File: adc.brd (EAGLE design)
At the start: 100 x 80 mm, 1 part, among them U1 ADV7173KSTZ

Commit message: placa ADC v1
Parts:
- added C1, C10, C12, C3, C5, C6, C7, C8, C9: 10nf, eagle-ltspice:C0603
- added C11, C13, C2, C4: 10uf, eagle-ltspice:C0603
- added D1, D2, D3, D4, D5, D6: PMLL4150, diode:SOD80C
- added IC13, IC5, IC6: 4051D, 40xx:SO16
- added JP1, JP2, JP3: (no value), jumper:JP2
- added R1, R10, R11, R12, R13, R14, R15, R16, R17, R18, R19, R2, R20, R21, R22, R23, R24, R25, R26, R27, R28, R29, R3, R30, R31, R32, R33, R34, R35, R36, R37, R38, R39, R4, R40, R41, R42, R43, R44, R45, R46, R47, R5, R6, R7, R8, R9: (no value), SparkFun:0603
- added SV1, SV2: (no value), con-lstb:MA20-2
- added U$1, U$2: POT100K_3362U, SparkFun:3362U
- added U2, U5, U6, U7: AD5308ARUZ, Analog Devices_By_element14_Batch_1:SOP65P640X120-16N
- added U3: AD7927BRUZ, Analog Devices_By_element14_Batch_1:SOP65P640X120-20N
- added U4: ADV7173KSTZ, ADI-Phase-2:QFP50P900X900X160-48N
- moved U1 30.4 mm to (19.1, 29.5), turned to 180 degrees
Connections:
- net VAA_3 renamed +IN_B
- removed net ALOHADANCE: U1.1
- removed net VAA: U1.46
- removed net VAA_4: U1.19
- removed net VAA_5: U1.27
- removed net VAA_6: U1.30
- removed net VAA_7: U1.32
- removed net VAA_8: U1.34
- new net +2,5V_ADCREF: U1.5, U1.7, U4.5, U4.7
- new net +INA: U2.3
- new net CH_A(ADC): D1.A, D2.C, R17.1, U1.2, U5.10
- new net CH_B(ADC): D3.A, D4.C, R33.1, U4.11, U6.10
- new net CH_C(ADC): D5.A, D6.C, R47.1, U4.2, U7.10
- new net DAC_OUT: R1.2, U$1.P$3, U2.1
- new net DCLK: U1.14, U1.47, U4.14, U4.47
- new net DFS/GAIN: JP1.2, U1.4, U4.4
- new net DGND: C12.2, C13.2, C3.2, C4.2, C5.2, JP1.3, JP2.3, JP3.3, U1.1, U1.12, U1.16, U1.27, U1.29, U1.32, U1.34, U1.45, U3.17, U3.2, U3.20, U3.3, U4.1, U4.12, U4.16, U4.27, U4.29, U4.32, U4.34, U4.45
- new net GND: C1.2, C10.2, C11.2, C2.2, C7.2, C9.2, D2.A, D4.A, D6.A, IC13.8, IC5.8, IC6.8, R19.2, R22.2, R32.2, R36.2, R46.2, R8.2, U1.3, U2.14, U4.3
- new net N$1: C7.1, R2.1, U2.5
- new net N$10: SV2.29, U1.42
- new net N$100: U5.1, U5.2
- new net N$101: R31.1, R32.1, U6.11
- new net N$102: R37.2, R38.2, R39.2, R40.2, R41.2, R42.2, R43.2, R44.2
- new net N$103: U6.1, U6.2
- new net N$104: R45.1, R46.1, U7.11
- new net N$105: U7.1, U7.2
- new net N$106: R35.1, U7.3
- new net N$107: R21.1, U6.3
- new net N$109: R20.2, R21.2, R34.2, R35.2, R6.2, R7.2, U$2.P$3, U2.16
- new net N$11: SV2.40, U1.24
- new net N$12: SV2.30, U1.19
- new net N$13: SV2.32, U1.20
- new net N$14: SV2.39, U1.37
- new net N$15: SV2.31, U1.41
- new net N$16: SV2.25, U1.44
- new net N$17: SV2.34, U1.21
- new net N$18: SV2.27, U1.43
- new net N$19: SV2.35, U1.39
- new net N$2: C6.1, R1.1, R2.2
- new net N$20: SV2.37, U1.38
- new net N$21: SV2.36, U1.22
- new net N$22: SV2.28, U1.18
- new net N$23: SV2.26, U1.17
- new net N$24: SV2.2, U3.4
- new net N$25: SV2.38, U1.23
- new net N$26: SV2.4, U3.5
- new net N$27: SV2.6, U3.6
- new net N$28: SV2.8, U3.7
- new net N$29: SV2.10, U3.8
- new net N$3: C5.1, U$1.P$1, U$1.P$2, U2.2, U3.1
- new net N$30: SV2.12, U3.9
- new net N$31: SV2.14, U3.10
- new net N$32: SV2.16, U3.11
- new net N$33: SV2.18, U3.12
- new net N$34: SV2.20, U3.13
- new net N$35: SV2.22, U3.14
- new net N$36: SV2.24, U3.15
- new net N$37: SV2.1, U3.16
- new net N$38: IC5.13, R9.1
- new net N$39: IC5.14, R10.1
- new net N$4: C6.2, R3.2, U2.6, U2.7
- new net N$40: IC5.15, R11.1
- new net N$41: IC5.1, R12.1
- new net N$42: IC5.12, R13.1
- new net N$43: IC5.5, R14.1
- new net N$44: IC5.2, R15.1
- new net N$45: IC5.4, R16.1
- new net N$46: IC6.13, R23.1
- new net N$47: IC6.14, R24.1
- new net N$48: R23.2, R24.2, R25.2, R26.2, R27.2, R28.2, R29.2, R30.2
- new net N$49: R10.2, R11.2, R12.2, R13.2, R14.2, R15.2, R16.2, R9.2
- new net N$5: C9.1, R4.1, U2.12
- new net N$50: R18.1, R19.1, U5.11
- new net N$51: IC5.3, R17.2, U5.12
- new net N$52: IC6.15, R25.1
- new net N$53: IC6.1, R26.1
- new net N$54: IC6.12, R27.1
- new net N$55: IC6.5, R28.1
- new net N$56: IC6.2, R29.1
- new net N$57: IC6.4, R30.1
- new net N$58: R31.2, U6.6, U6.7
- new net N$59: R45.2, U7.6, U7.7
- new net N$6: C8.1, R3.1, R4.2
- new net N$60: IC13.3, R47.2, U7.12
- new net N$61: IC6.3, R33.2, U6.12
- new net N$62: IC13.13, R37.1
- new net N$63: IC13.14, R38.1
- new net N$64: IC13.15, R39.1
- new net N$65: IC13.1, R40.1
- new net N$66: IC13.12, R41.1
- new net N$67: IC13.5, R42.1
- new net N$68: IC13.2, R43.1
- new net N$69: IC13.4, R44.1
- new net N$7: C8.2, R5.2, U2.10, U2.11
- new net N$70: R34.1, R36.1, U7.5
- new net N$71: R6.1, R8.1, U5.5
- new net N$72: R20.1, R22.1, U6.5
- new net N$73: R7.1, U5.3
- new net N$74: SV1.33, U4.40
- new net N$75: SV1.29, U4.42
- new net N$76: SV1.40, U4.24
- new net N$77: SV1.30, U4.19
- new net N$78: SV1.32, U4.20
- new net N$79: SV1.39, U4.37
- new net N$8: R5.1, U$2.P$1, U$2.P$2, U2.15
- new net N$80: SV1.31, U4.41
- new net N$81: SV1.25, U4.44
- new net N$82: SV1.34, U4.21
- new net N$83: SV1.27, U4.43
- new net N$84: SV1.35, U4.39
- new net N$85: SV1.37, U4.38
- new net N$86: SV1.36, U4.22
- new net N$87: SV1.28, U4.18
- new net N$88: SV1.26, U4.17
- new net N$89: SV1.38, U4.23
- new net N$9: SV2.33, U1.40
- new net N$90: IC5.9, SV2.3
- new net N$91: IC5.10, SV2.5
- new net N$92: IC5.11, SV2.7
- new net N$93: IC13.9, SV1.1
- new net N$94: IC13.10, SV1.3
- new net N$95: IC13.11, SV1.5
- new net N$96: IC6.9, SV1.7
- new net N$97: IC6.10, SV1.9
- new net N$98: IC6.11, SV1.11
- new net N$99: R18.2, U5.6, U5.7
- new net S1: JP2.2, U1.8, U4.8
- new net S2: JP3.2, U1.9, U4.9
- new net VCC: C1.1, C10.1, C11.1, C2.1, D1.C, D3.C, D5.C, IC13.16, IC13.6, IC5.16, IC5.6, IC6.16, IC6.6, U1.13, U1.30, U1.31, U1.48, U4.13, U4.31, U4.48
- new net VD1: U4.30
- new net VDD: C12.1, C13.1, C3.1, C4.1, JP1.1, JP2.1, JP3.1, U1.15, U1.28, U1.33, U1.46, U2.13, U2.4, U3.18, U3.19, U4.15, U4.28, U4.33, U4.46, U5.13, U5.4, U6.13, U6.4, U7.13, U7.4
- new net VEE: IC13.7, IC5.7, IC6.7
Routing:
- net DGND: track 0.00 -> 92.1 mm
- net VDD: track 0.00 -> 87.1 mm, vias 0 -> 4
- net N$109: track 0.00 -> 78.7 mm
- net GND: track 0.00 -> 73.3 mm, vias 0 -> 3
- net S2: track 0.00 -> 71.0 mm, vias 0 -> 1
- net DFS/GAIN: track 0.00 -> 70.1 mm, vias 0 -> 1
- net CH_B(ADC): track 0.00 -> 65.1 mm, vias 0 -> 1
- net N$102: track 0.00 -> 45.2 mm
- net CH_C(ADC): track 0.00 -> 44.8 mm, vias 0 -> 2
- net CH_A(ADC): track 0.00 -> 43.2 mm
- net N$48: track 0.00 -> 40.6 mm
- net N$73: track 0.00 -> 37.0 mm, vias 0 -> 2
- net VCC: track 0.00 -> 34.0 mm
- net N$51: track 0.00 -> 33.0 mm, vias 0 -> 2
- net N$60: track 0.00 -> 31.4 mm, vias 0 -> 2
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- added copper zone on layer 1, net GND

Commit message: VHDL
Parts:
- removed D1, D2, D3, D4, D5, D6: PMLL4150, diode:SOD80C
- moved SV2 26.2 mm to (50.5, 2.54)
- moved JP3 25.5 mm to (30.0, 47.2), turned to 90 degrees
- moved JP1 19.9 mm to (25.9, 47.2), turned to 90 degrees
- moved JP2 15.0 mm to (21.8, 47.2), turned to 90 degrees
- moved SV1 14.7 mm to (4.57, 54.9)
- moved R17 13.1 mm to (51.3, 22.1)
- moved R18 13.0 mm to (57.1, 22.1)
- moved U5 12.8 mm to (53.8, 29.0)
- moved R19 12.2 mm to (54.4, 20.8)
- moved C4 11.3 mm to (19.1, 57.7)
- moved C3 10.6 mm to (21.1, 57.7)
- moved C1 10.6 mm to (35.3, 56.6)
- moved U$1 10.2 mm to (60.7, 21.8)
- moved C2 10.1 mm to (37.3, 56.6)
- moved C13 9.81 mm to (18.8, 31.2)
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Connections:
- removed net N$85: SV1.37, U4.38
- removed net N$92: IC5.11, SV2.7
- new net +5V: SV1.30, SV2.30, U2.4, U5.4, U6.4, U7.4
- new net -5V: U2.13, U5.13, U6.13, U7.13
- new net N$110: IC5.11, SV2.20
- new net N$111: SV2.16, U3.16
- net CH_A(ADC): no longer D1.A, D2.C
- net CH_B(ADC): no longer D3.A, D4.C
- net CH_C(ADC): no longer D5.A, D6.C
- net DGND: now also SV1.11, SV1.12, SV2.11, SV2.12
- net GND: no longer D2.A, D4.A, D6.A
- net N$10: now also SV2.25; no longer SV2.29
- net N$11: now also SV2.39; no longer SV2.40
- net N$12: now also SV2.32; no longer SV2.30
- net N$13: now also SV2.34; no longer SV2.32
- net N$14: now also SV2.37; no longer SV2.39
- net N$15: now also SV2.27; no longer SV2.31
- net N$16: now also SV2.21; no longer SV2.25
- net N$17: now also SV2.36; no longer SV2.34
- net N$18: now also SV2.23; no longer SV2.27
- net N$19: now also SV2.33; no longer SV2.35
- net N$20: now also SV2.35; no longer SV2.37
- net N$21: now also SV2.38; no longer SV2.36
- net N$24: now also SV2.13; no longer SV2.2
- net N$25: now also SV2.40; no longer SV2.38
- net N$26: now also SV2.9; no longer SV2.4
- net N$27: now also SV2.7; no longer SV2.6
- net N$28: now also SV2.5; no longer SV2.8
- net N$29: now also SV2.3; no longer SV2.10
- net N$30: now also SV2.1; no longer SV2.12
- net N$31: now also SV2.2; no longer SV2.14
- net N$32: now also SV2.4; no longer SV2.16
- net N$33: now also SV2.6; no longer SV2.18
- net N$34: now also SV2.8; no longer SV2.20
- net N$35: now also SV2.10; no longer SV2.22
- net N$36: now also SV2.14; no longer SV2.24
- net N$37: now also SV1.38, U4.37; no longer SV2.1, U3.16
- net N$74: now also SV1.40, U4.38; no longer SV1.33, U4.40
- net N$75: now also SV1.39, U4.39; no longer SV1.29, U4.42
- net N$76: now also SV1.36; no longer SV1.40
- net N$77: now also SV1.24; no longer SV1.30
- net N$78: now also SV1.26; no longer SV1.32
- net N$79: now also SV1.37, U4.40; no longer SV1.39, U4.37
- net N$80: now also SV1.35; no longer SV1.31
- net N$81: now also SV1.33, U4.42; no longer SV1.25, U4.44
- net N$82: now also SV1.28; no longer SV1.34
- net N$83: now also SV1.31; no longer SV1.27
- net N$84: now also SV1.27, U4.44; no longer SV1.35, U4.39
- net N$86: now also SV1.32; no longer SV1.36
- net N$87: now also SV1.22; no longer SV1.28
- net N$88: now also SV1.20; no longer SV1.26
- net N$89: now also SV1.34; no longer SV1.38
- net N$9: now also SV2.31; no longer SV2.33
- net N$90: now also SV2.24; no longer SV2.3
- net N$91: now also SV2.22; no longer SV2.5
- net N$93: now also SV1.19; no longer SV1.1
- net N$94: now also SV1.15; no longer SV1.3
- net N$95: now also SV1.13; no longer SV1.5
- net N$96: now also SV1.25; no longer SV1.7
- net N$97: now also SV1.23; no longer SV1.9
- net N$98: now also SV1.21; no longer SV1.11
- net VCC: no longer D1.C, D3.C, D5.C
- net VDD: now also SV1.29, SV2.29; no longer U2.13, U2.4, U5.13, U5.4, U6.13, U6.4, U7.13, U7.4
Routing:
- net +5V: track 0.00 -> 248.5 mm, vias 0 -> 4
- net VDD: track 87.1 -> 295.7 mm, vias 4 -> 5
- net VCC: track 34.0 -> 238.2 mm, vias 0 -> 12
- net DGND: track 92.1 -> 275.2 mm, vias 0 -> 5
- net VEE: track 0.00 -> 139.6 mm, vias 0 -> 3
- net GND: track 73.3 -> 169.2 mm, vias 3 -> 12
- net N$23: track 0.00 -> 86.8 mm
- net N$22: track 0.00 -> 81.2 mm
- net N$98: track 0.00 -> 80.7 mm, vias 0 -> 1
- net -5V: track 0.00 -> 79.5 mm, vias 0 -> 4
- net N$97: track 0.00 -> 74.9 mm, vias 0 -> 1
- net N$12: track 0.00 -> 71.8 mm
- net N$96: track 0.00 -> 71.6 mm, vias 0 -> 1
- net N$84: track 0.00 -> 71.3 mm
- net N$93: track 0.00 -> 70.4 mm
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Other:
- board size 100 x 80 mm -> 87.6 x 89.9 mm

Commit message: autalização
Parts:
- added X1: (no value), con-ptr500:AK300/5
- moved SV1 3.90 mm to (1.27, 56.9)
- moved U4 3.58 mm to (24.5, 61.3)
- moved C3 3.16 mm to (18.2, 58.9)
- moved C4 3.16 mm to (16.1, 58.9)
- moved C1 3.14 mm to (32.4, 57.8)
- moved C2 3.14 mm to (34.4, 57.8)
- moved C5 2.40 mm to (59.9, 21.8), turned to 180 degrees
- moved R29 2.34 mm to (46.5, 52.1)
- moved R30 1.89 mm to (46.4, 54.2)
- moved IC6 1.76 mm to (39.3, 48.4)
- moved R28 1.49 mm to (46.4, 56.3)
- moved R26 1.22 mm to (45.9, 48.5)
- moved C13 1.12 mm to (19.8, 30.7)
- moved C12 0.92 mm to (21.6, 30.7)
- moved U1 0.89 mm to (27.7, 32.6)
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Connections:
- removed net DGND: C12.2, C13.2, C3.2, C4.2, C5.2, JP1.3, JP2.3, JP3.3, SV1.11, SV1.12, SV2.11, SV2.12, U1.1, U1.12, U1.16, U1.27, U1.29, U1.32, U1.34, U1.45, U3.17, U3.2, U3.20, U3.3, U4.1, U4.12, U4.16, U4.27, U4.29, U4.32, U4.34, U4.45
- net +2,5V_ADCREF: now also X1.3
- net +5V: now also X1.5
- net -5V: now also X1.4
- net DCLK: now also SV1.10
- net GND: now also C12.2, C13.2, C3.2, C4.2, C5.2, JP1.3, JP2.3, JP3.3, SV1.11, SV1.29, SV2.11, SV2.29, U1.1, U1.12, U1.16, U1.27, U1.29, U1.32, U1.34, U1.45, U3.17, U3.2, U3.20, U3.3, U4.1, U4.12, U4.27, U4.29, U4.32, U4.34, U4.45, X1.1
- net N$93: now also SV1.17; no longer SV1.19
- net VDD: now also SV1.12, SV2.12, X1.2; no longer SV1.29, SV2.29
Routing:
- net GND: track 169.2 -> 475.0 mm, vias 12 -> 19
- net DGND: track 275.2 -> 0.00 mm, vias 5 -> 0
- net -5V: track 79.5 -> 142.3 mm
- net +5V: track 248.5 -> 309.9 mm
- net DCLK: track 68.3 -> 115.1 mm, vias 2 -> 3
- net VDD: track 295.7 -> 335.1 mm
- net +2,5V_ADCREF: track 45.6 -> 79.7 mm, vias 2 -> 4
- net N$102: track 45.2 -> 18.5 mm
- net VEE: track 139.6 -> 161.6 mm
- net S2: track 59.2 -> 41.2 mm
- net N$48: track 35.6 -> 19.2 mm
- net N$95: track 64.4 -> 72.4 mm
- net N$23: track 86.8 -> 94.6 mm
- net N$98: track 80.7 -> 87.4 mm
- net N$94: track 67.1 -> 73.6 mm
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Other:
- board size 87.6 x 89.9 mm -> 96.2 x 95.5 mm

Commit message: Atualização
VHDL com SWITCH CASE. 1-16 start end package
C# com controle de erro
ADC com alterações
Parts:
- removed X1: (no value), con-ptr500:AK300/5
- added X2: (no value), con-ptr500:AK300/6
- moved R45 3.84 mm to (54.1, 63.0), turned to 180 degrees
- moved C13 3.07 mm to (19.8, 27.6)
- moved R33 1.81 mm to (50.7, 41.9)
- moved R21 1.78 mm to (66.5, 54.4)
- moved R46 1.30 mm to (56.6, 65.5)
- moved R12 1.24 mm to (44.7, 22.1)
- moved R14 1.24 mm to (44.7, 29.4)
- moved R15 1.24 mm to (44.7, 24.6)
- moved R16 1.24 mm to (44.7, 27.2)
- moved R20 1.22 mm to (66.5, 50.7)
- moved R22 1.19 mm to (62.7, 50.7)
- moved C12 0.54 mm to (21.1, 30.7)
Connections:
- removed net N$100: U5.1, U5.2
- removed net N$103: U6.1, U6.2
- removed net N$105: U7.1, U7.2
- removed net VD1: U4.30
- new net 1V: U3.19, X2.2
- net +2,5V_ADCREF: now also X2.3; no longer X1.3
- net +5V: now also SV1.12, SV2.12, X2.5; no longer SV1.30, SV2.30, X1.5
- net -5V: now also X2.4; no longer X1.4
- net GND: now also X2.1; no longer X1.1
- net N$102: now also U7.1, U7.2
- net N$110: now also SV2.15; no longer SV2.20
- net N$48: now also U6.1, U6.2
- net N$49: now also U5.1, U5.2
- net N$90: now also SV2.19; no longer SV2.24
- net N$91: now also SV2.17; no longer SV2.22
- net VCC: now also U4.30
- net VDD: now also SV1.30, SV2.30, X2.6; no longer SV1.12, SV2.12, U3.19, X1.2
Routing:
- net GND: track 475.0 -> 1079.7 mm, vias 19 -> 21
- net VCC: track 244.6 -> 463.0 mm, vias 10 -> 11
- net 1V: track 0.00 -> 119.7 mm
- net N$48: track 19.2 -> 82.8 mm, vias 0 -> 2
- net N$49: track 17.5 -> 59.0 mm, vias 0 -> 2
- net N$102: track 18.5 -> 39.4 mm, vias 0 -> 2
- net N$59: track 14.9 -> 35.3 mm
- net DCLK: track 115.1 -> 135.1 mm
- net +2,5V_ADCREF: track 79.7 -> 94.1 mm
- net -5V: track 142.3 -> 156.3 mm
- net +5V: track 309.9 -> 323.6 mm, vias 4 -> 5
- net S2: track 41.2 -> 54.2 mm
- net CH_C(ADC): track 40.9 -> 51.5 mm
- net N$8: track 9.67 -> 19.6 mm
- net VEE: track 161.6 -> 170.3 mm
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- added copper zone on layer 16, net GND
- removed copper zone on layer 1, net GND
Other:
- board size 96.2 x 95.5 mm -> 96 x 95.3 mm

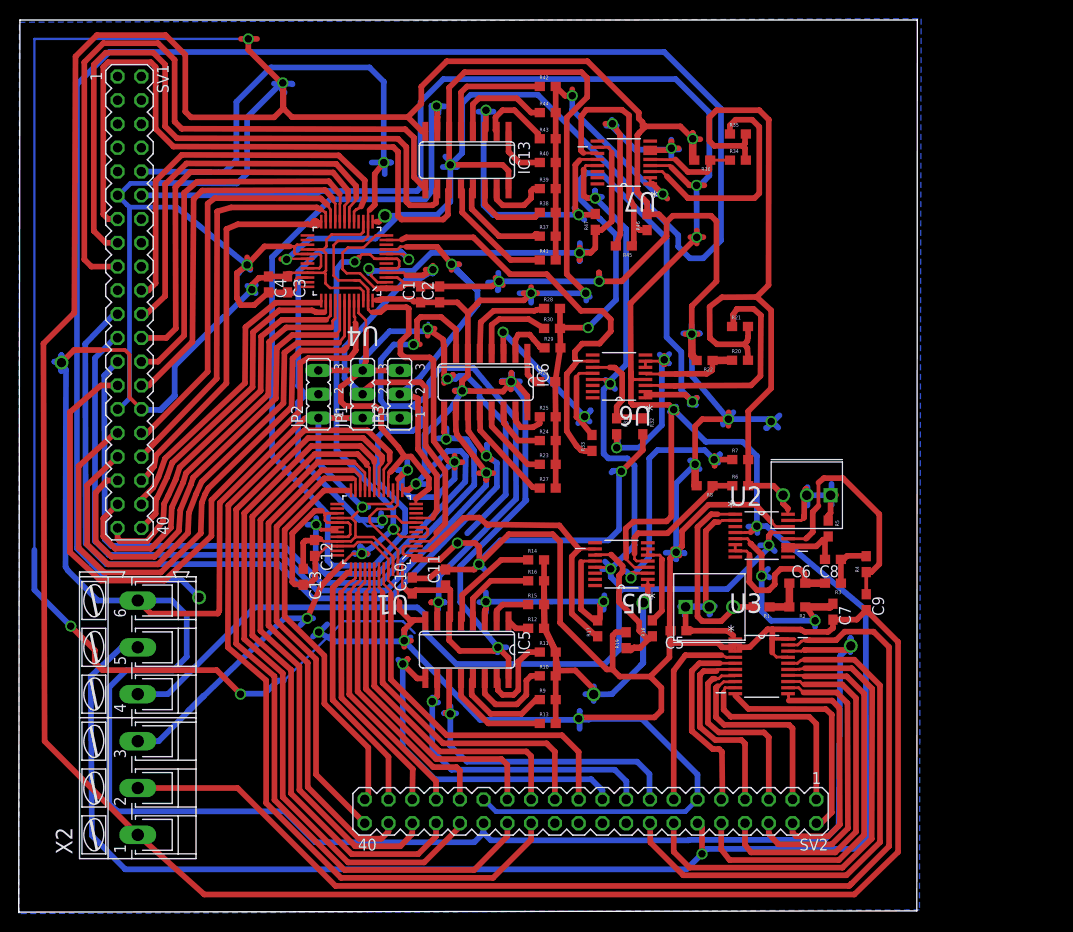
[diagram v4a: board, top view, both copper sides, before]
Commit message: ADC update
Atualizado algumas trilhas e GND não conectado
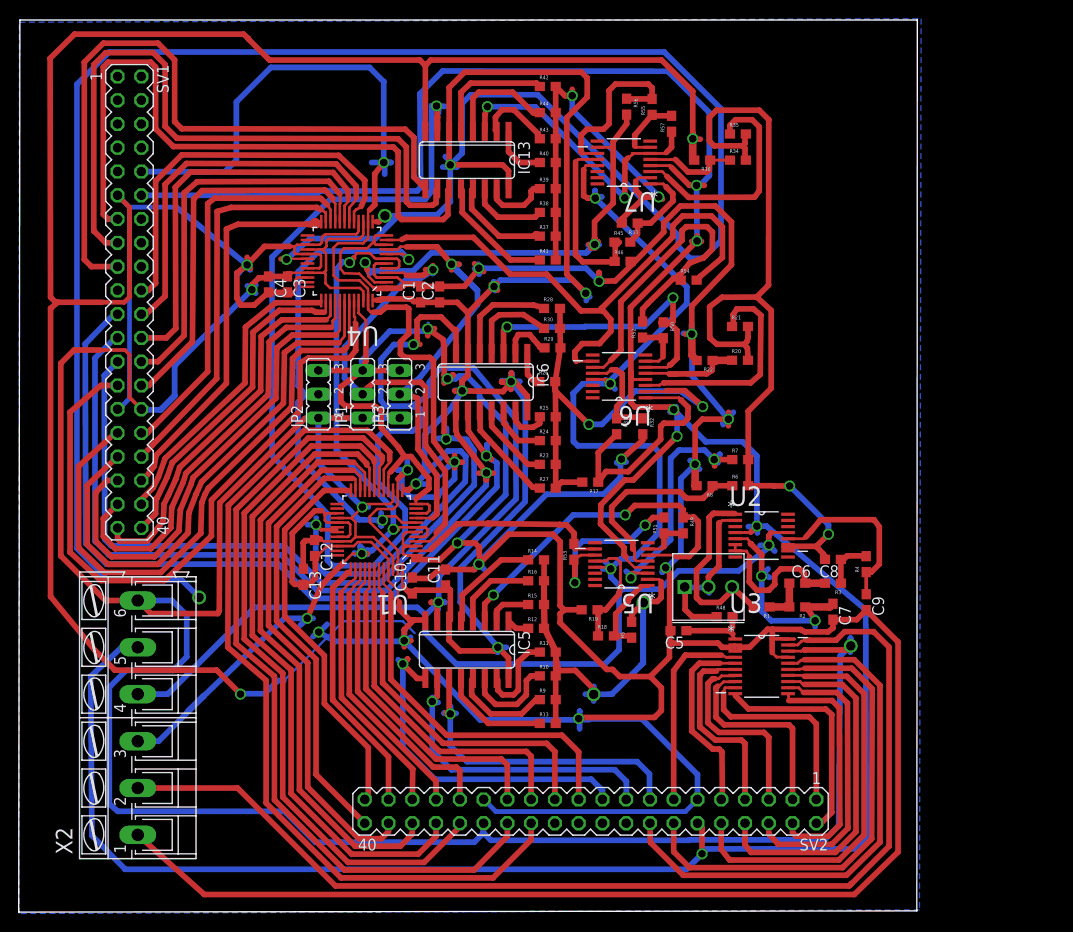
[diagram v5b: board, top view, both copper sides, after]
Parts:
- removed R47: (no value), SparkFun:0603
- removed U$2: POT100K_3362U, SparkFun:3362U
- added R48, R49, R50, R51, R52, R53, R54, R55, R56, R57: (no value), SparkFun:0603
- moved R33 23.8 mm to (54.7, 65.4), turned to 180 degrees
- moved R5 23.6 mm to (54.9, 21.9), turned to 90 degrees
- moved R17 15.6 mm to (50.5, 37.7), turned to 180 degrees
- moved R19 5.09 mm to (50.4, 24.1), turned to 180 degrees
- moved R18 5.02 mm to (52.2, 21.3), turned to 0 degrees
- moved R46 4.94 mm to (54.0, 61.3), turned to 0 degrees
- moved U$1 2.14 mm to (60.6, 24.0)
- moved R45 0.43 mm to (53.9, 63.4), turned to 0 degrees
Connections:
- removed net N$109: R20.2, R21.2, R34.2, R35.2, R6.2, R7.2, U$2.P$3, U2.16
- removed net N$59: R45.2, U7.6, U7.7
- removed net VEE: IC13.7, IC5.7, IC6.7
- new net N$103: C5.1, R48.2, U3.1
- new net N$105: R18.2, R5.1, U5.1
- new net N$114: R55.2, R56.1, U7.11
- new net N$117: R51.2, R53.1, U5.11
- new net N$119: R55.1, R57.2, U7.7
- new net N$120: R17.1, R31.2, U6.1
- new net N$121: R50.2, R52.1, U6.7
- new net N$122: IC6.3, R50.1, U6.6
- net -5V: now also IC13.7, IC5.7, IC6.7
- net CH_A(ADC): now also R53.2; no longer R17.1
- net CH_B(ADC): now also R54.2; no longer R33.1
- net CH_C(ADC): now also R56.2; no longer R47.1
- net GND: now also U1.10, U1.6, U4.10, U4.16, U4.6; no longer U2.14
- net N$101: now also U6.12; no longer U6.11
- net N$102: now also R33.2; no longer U7.1
- net N$104: now also U7.12; no longer U7.11
- net N$3: now also R48.1; no longer C5.1, U3.1
- net N$48: now also R17.2; no longer U6.1
- net N$49: now also R5.2; no longer U5.1
- net N$50: now also U5.12; no longer U5.11
- net N$51: now also R49.2, R51.1, U5.7; no longer IC5.3, R17.2, U5.12
- net N$58: now also R52.2, R54.1, U6.11; no longer R31.2, U6.6, U6.7
- net N$60: now also R33.1, R45.2, U7.1; no longer IC13.3, R47.2, U7.12
- net N$61: now also IC13.3, R57.1, U7.6; no longer IC6.3, R33.2, U6.12
- net N$7: now also R20.2, R21.2, R34.2, R35.2, R6.2, R7.2; no longer R5.2
- net N$8: now also U2.14; no longer R5.1, U$2.P$1, U$2.P$2, U2.15
- net N$99: now also IC5.3, R49.1; no longer R18.2, U5.7
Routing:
- net -5V: track 156.3 -> 344.7 mm, vias 4 -> 7
- net VEE: track 170.3 -> 0.00 mm, vias 3 -> 0
- net GND: track 1079.7 -> 923.6 mm, vias 21 -> 17
- net N$7: track 9.74 -> 97.6 mm, vias 0 -> 2
- net N$109: track 80.8 -> 0.00 mm
- net N$59: track 35.3 -> 0.00 mm, vias 2 -> 0
- net N$122: track 0.00 -> 34.6 mm, vias 0 -> 2
- net N$48: track 82.8 -> 49.4 mm
- net N$60: track 41.4 -> 10.7 mm, vias 2 -> 0
- net N$99: track 9.43 -> 38.8 mm, vias 0 -> 2
- net N$51: track 32.2 -> 5.43 mm, vias 2 -> 0
- net N$120: track 0.00 -> 25.5 mm
- net N$8: track 19.6 -> 0.00 mm
- net N$114: track 0.00 -> 19.6 mm
- net N$117: track 0.00 -> 19.4 mm, vias 0 -> 2
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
